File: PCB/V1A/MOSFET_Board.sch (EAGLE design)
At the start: 276 parts, among them IC301 7805T, IC302 7805T, J301 +12V, J302 FAN_MOLEX4PIN, J303 FAN_MOLEX4PIN, J304 DUT+, J305 DUT-, Q201 SIRC10DP, Q202 SIRC10DP, Q203 BC817, Q204 BC817, Q205 SIRC10DP, Q206 SIRC10DP, Q207 BC817, Q208 BC807, Q209 BC817, Q210 BC807, Q211 IXTK102N65X2, Q212 IXTK102N65X2, Q301 BC817, Q302 BC817, Q401 BC807, Q402 BC807, Q403 BC807, Q404 BC807, Q405 BC807, Q406 BC807, Q407 BC807, Q408 BC807, Q409 BC807, Q410 BC807, Q411 BC807, Q412 BC807, Q413 BC807, Q414 BC807, U1 LP2985-3.1, U201 AD420, U202 AD420, U203 LT1014I, U204 LT1014I, U205 AD620, U206 AD620, U207 AD620, U208 AD620, U209 LTC1865L, U210 LTC1865L, U301 LP2985-3.1, U302 LP2985-3.1, U303 AD620, U304 LTC1865L, U305 LTC1865L, U306 MAX743, U401 HCPL-063N, U402 HCPL-063N, U403 HCPL-063N, U404 HCPL-063N, U405 HCPL-063N, U406 HCPL-063N, U407 HCPL-063N

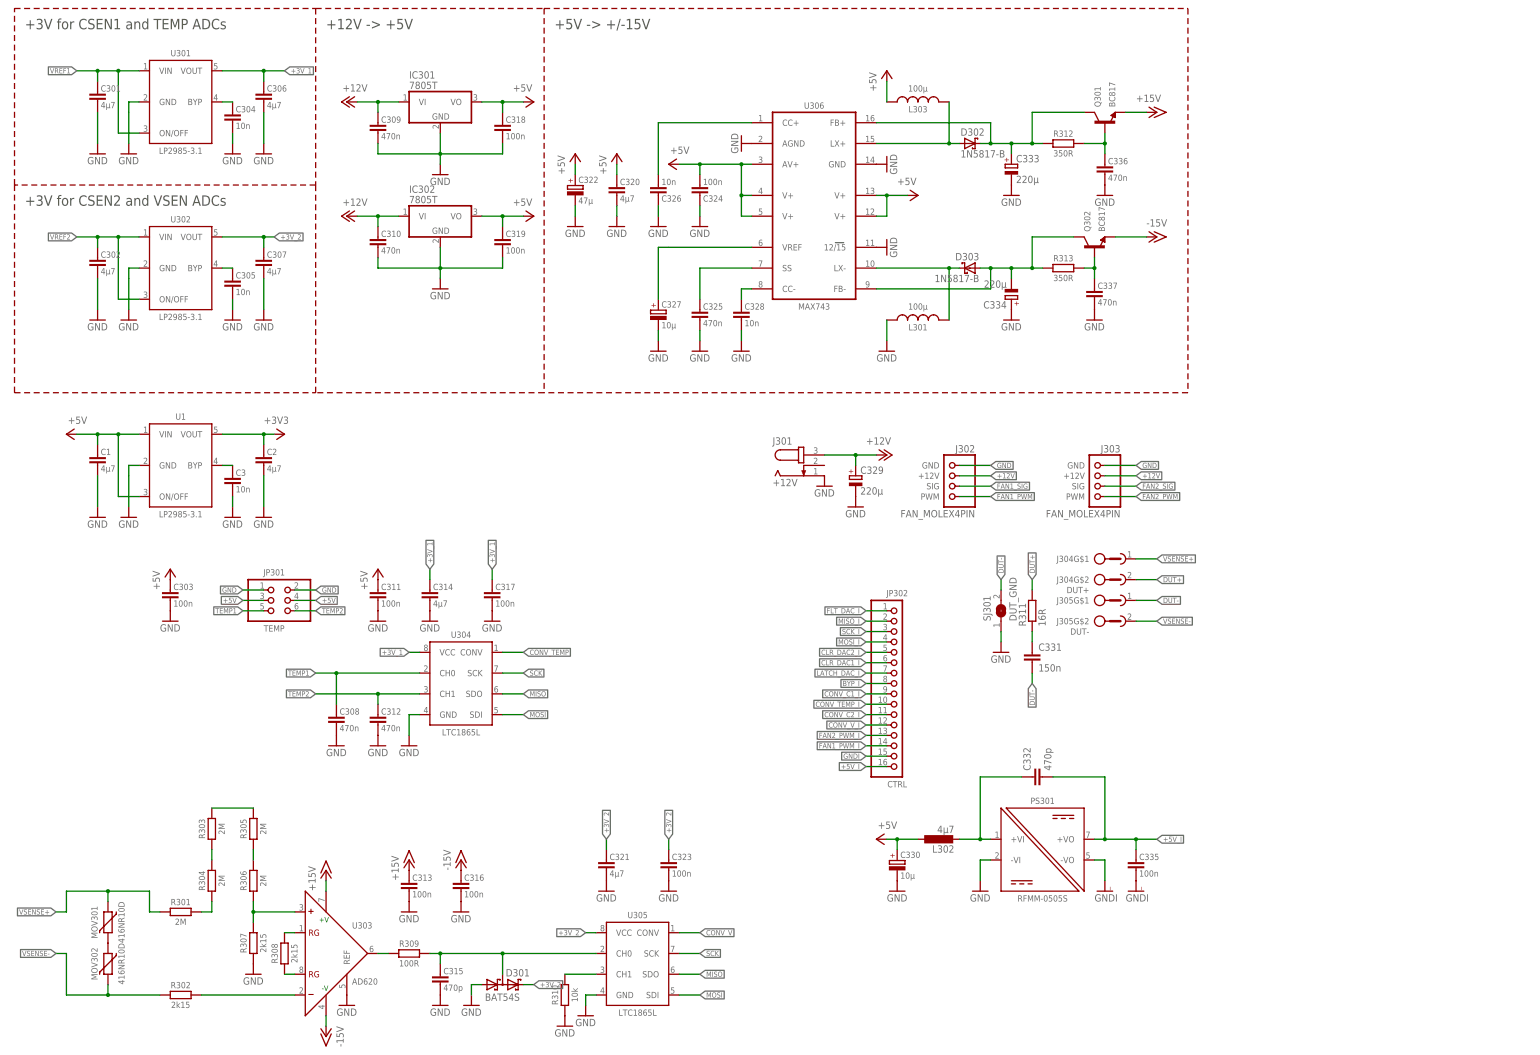
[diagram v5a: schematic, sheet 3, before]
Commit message: Finished first pass routing/layout
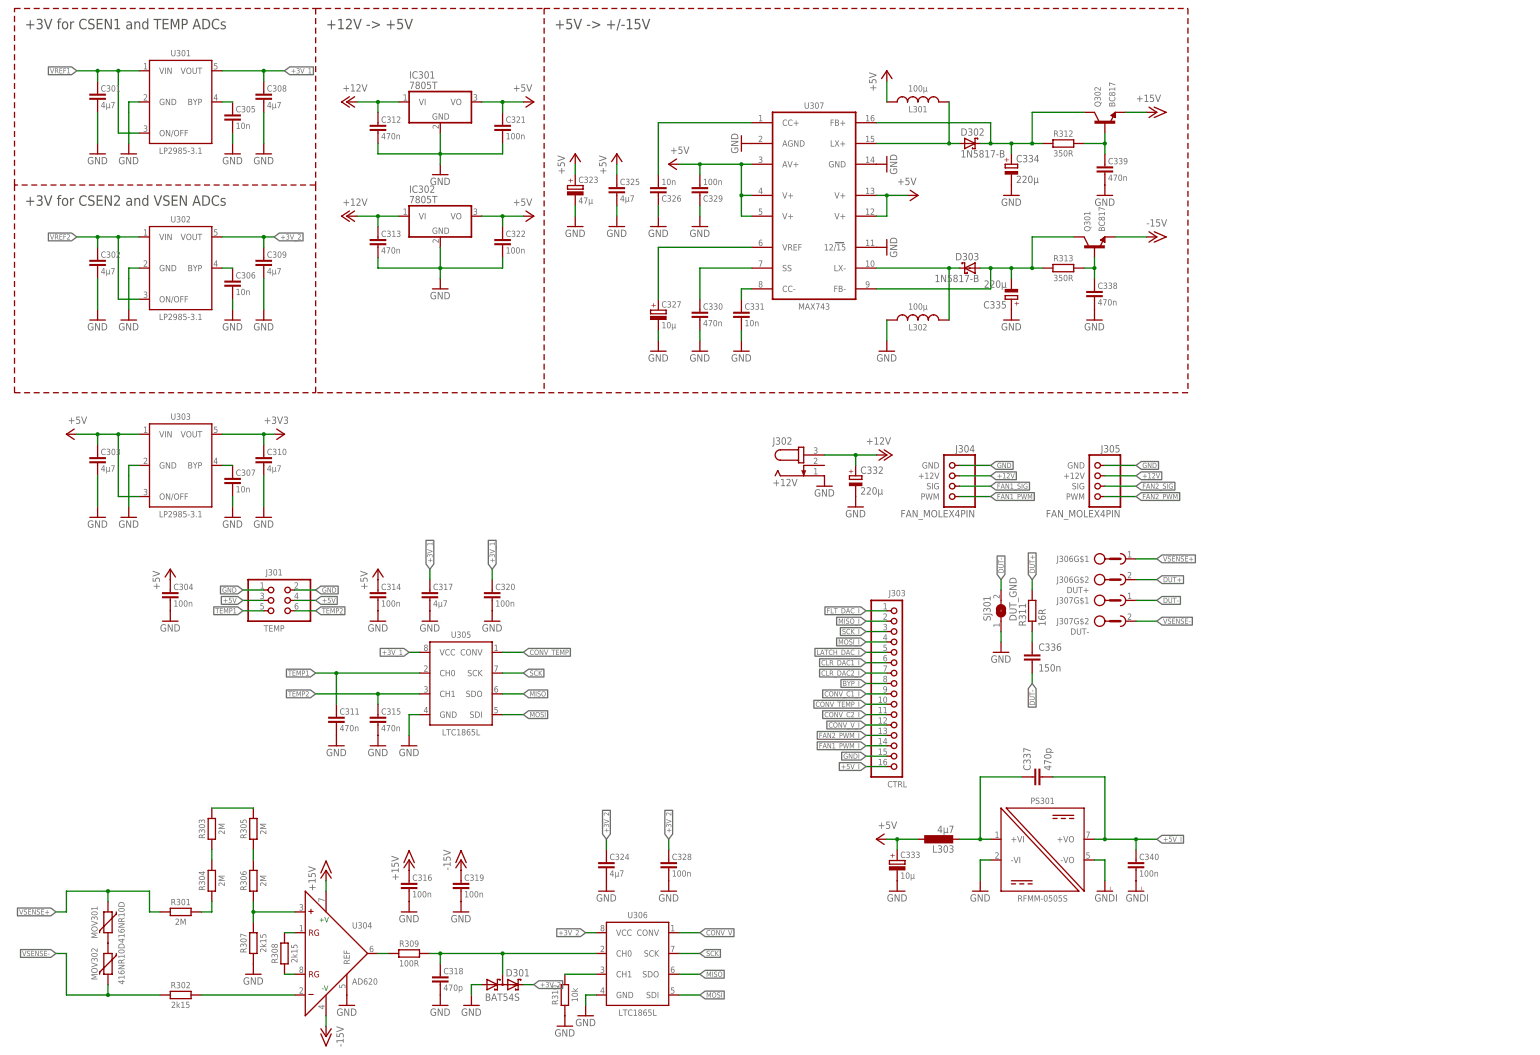
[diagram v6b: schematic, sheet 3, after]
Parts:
- removed C1, C2: 4µ7, passives:C-EU-3216
- removed C3: 10n, passives:C-EU-2012
- removed JP301: TEMP, mechanical:HEAD_2X3_MALE
- removed JP302: CTRL, mechanical:HEAD_1X16_MALE
- removed U1: LP2985-3.1, ic:LP2985-3.1
- added C338, C339: 470n, passives:C-EU-1608
- added C340: 100n, passives:C-EU-1608
- added J306: DUT+, mechanical:AMPHENOL_TERM-BLOCK_2
- added J307: DUT-, mechanical:AMPHENOL_TERM-BLOCK_2
- added U307: MAX743, ic:MAX743WE
- C303, C317, C324: value 100n -> 4µ7; device passives:C-EU-1608 -> passives:C-EU-3216
- C304, C328: value 10n -> 100n; device passives:C-EU-2012 -> passives:C-EU-1608
- C306, C307: value 4µ7 -> 10n; device passives:C-EU-3216 -> passives:C-EU-2012
- C308, C309, C310, C325: value 470n -> 4µ7; device passives:C-EU-1608 -> passives:C-EU-3216
- C311, C313: value 100n -> 470n
- C314, C320, C321: value 4µ7 -> 100n; device passives:C-EU-3216 -> passives:C-EU-1608
- C315: value 470p -> 470n
- C318: value 100n -> 470p
- C322: value 47µ -> 100n; device passives:CPOL-7343-DE -> passives:C-EU-1608
- C323: value 100n -> 47µ; device passives:C-EU-1608 -> passives:CPOL-7343-DE
- C329: value 220µ -> 100n; device rcl:CPOL-EUE3.5-10 -> passives:C-EU-1608
- C330: value 10µ -> 470n; device passives:CPOL-6032-C -> passives:C-EU-1608
- C331: value 150n -> 10n; device rcl:C-EU050-030X075 -> passives:C-EU-2012
- C332: value 470p -> 220µ; device rcl:C-EU075-032X103 -> rcl:CPOL-EUE3.5-10
- C333: value 220µ -> 10µ; device rcl:CPOL-EUE3.5-10 -> passives:CPOL-6032-C
- C335: value 100n -> 220µ; device passives:C-EU-1608 -> rcl:CPOL-EUE3.5-10
- C336: value 470n -> 150n; device passives:C-EU-1608 -> rcl:C-EU050-030X075
- C337: value 470n -> 470p; device passives:C-EU-1608 -> rcl:C-EU075-032X103
- J301: value +12V -> TEMP; device con-jack:JACK-PLUG1 -> mechanical:HEAD_2X3_MALE
- J302: value FAN_MOLEX4PIN -> +12V; device mechanical:FAN_MOLEX4PIN -> con-jack:JACK-PLUG1
- J303: value FAN_MOLEX4PIN -> CTRL; device mechanical:FAN_MOLEX4PIN -> mechanical:HEAD_1X16_MALE
- J304: value DUT+ -> FAN_MOLEX4PIN; device mechanical:AMPHENOL_TERM-BLOCK_2 -> mechanical:FAN_MOLEX4PIN
- J305: value DUT- -> FAN_MOLEX4PIN; device mechanical:AMPHENOL_TERM-BLOCK_2 -> mechanical:FAN_MOLEX4PIN
- L302: value 4µ7 -> 100µ; device inductor-coilcraft:MSS7341 -> passives:L-EU_MSS1260
- L303: value 100µ -> 4µ7; device passives:L-EU_MSS1260 -> inductor-coilcraft:MSS7341
- U303: value AD620 -> LP2985-3.1; device ic:AD620R-8 -> ic:LP2985-3.1
- U304: value LTC1865L -> AD620; device ic:LTC1865L -> ic:AD620R-8
- U306: value MAX743 -> LTC1865L; device ic:MAX743WE -> ic:LTC1865L
- renumbered HS1 to HS201, HS2 to HS202
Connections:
- net +12V: now also C312.1, C313.1, C332.+, J302.3, J304.+12V, J305.+12V; no longer C309.1, C310.1, C329.+, J301.3, J302.+12V, J303.+12V
- net +15V: now also C316.1, Q302.E, U304.+V; no longer C313.1, Q301.E, U303.+V
- net +3V3: now also C310.1, U303.VOUT; no longer C2.1, U1.VOUT
- net +3V_1: now also C308.1, C320.1, U305.VCC; no longer C306.1, C314.1, U304.VCC
- net +3V_2: now also C309.1, C324.1, C328.1, U306.VCC; no longer C307.1, C321.1, C323.1, U305.VCC
- net +5V: now also C304.1, C314.1, C321.1, C322.1, C323.+, C325.1, C329.2, C333.+, J301.3, J301.4, L301.1, L303.2, U303.ON/OFF, U303.VIN, U307.AV+, U307.V+, U307.V+@1, U307.V+@2, U307.V+@3; no longer C1.1, C311.1, C318.1, C319.1, C320.1, C322.+, C324.2, C330.+, JP301.3, JP301.4, L302.2, L303.1, U1.ON/OFF, U1.VIN, U306.AV+, U306.V+, U306.V+@1, U306.V+@2, U306.V+@3
- net +5V_I: now also C337.2, C340.1, J303.16; no longer C332.2, C335.1, JP302.16
- net -15V: now also C319.1, Q301.E, U304.-V; no longer C316.1, Q302.E, U303.-V
- net BYP_I: now also J303.8; no longer JP302.8
- net CLR_DAC1_I: now also J303.6; no longer JP302.6
- net CLR_DAC2: now also C413.1, R413.1, U401.VO2; no longer C427.1, R427.1, U406.VO2
- net CLR_DAC2_I: now also J303.7, Q405.B; no longer JP302.5, Q413.B
- net CONV_C1_I: now also J303.9; no longer JP302.9
- net CONV_C2_I: now also J303.11; no longer JP302.11
- net CONV_TEMP: now also U305.CONV; no longer U304.CONV
- net CONV_TEMP_I: now also J303.10; no longer JP302.10
- net CONV_V: now also U306.CONV; no longer U305.CONV
- net CONV_V_I: now also J303.12; no longer JP302.12
- net DUT+: now also J306G$2.1; no longer J304G$2.1
- net DUT-: now also C336.2, J307G$1.1; no longer C331.2, J305G$1.1
- net FAN1_PWM: now also J304.PWM; no longer J302.PWM
- net FAN1_PWM_I: now also J303.14; no longer JP302.14
- net FAN1_SIG: now also J304.SIG; no longer J302.SIG
- net FAN2_PWM: now also J305.PWM; no longer J303.PWM
- net FAN2_PWM_I: now also J303.13; no longer JP302.13
- net FAN2_SIG: now also J305.SIG; no longer J303.SIG
- net FLT_DAC_I: now also J303.1; no longer JP302.1
- net GND: now also C322.2, C323.-, C324.2, C329.1, C330.2, C331.2, C332.-, C334.-, C335.+, C338.2, C339.2, J301.2, J302.1, J304.GND, J305.GND, L302.2, U303.GND, U304.REF, U307.12/15, U307.AGND, U307.GND; no longer C1.2, C2.2, C3.2, C322.-, C323.2, C324.1, C329.-, C330.-, C334.+, C336.2, C337.2, J302.GND, J303.GND, JP301.1, JP301.2, L301.2, U1.GND, U303.REF, U304.GND, U306.12/15, U306.AGND
- net GNDI: now also C340.2, J303.15; no longer C335.2, JP302.15
- net LATCH_DAC: now also C427.1, R427.1, U406.VO2; no longer C413.1, R413.1, U401.VO2
- net LATCH_DAC_I: now also J303.5, Q413.B; no longer JP302.7, Q405.B
- net MISO: now also U306.SDO; no longer U304.SDO
- net MISO_I: now also J303.2; no longer JP302.2
- net MOSI: now also U306.SDI; no longer U304.SDI
- net MOSI_I: now also J303.4; no longer JP302.4
- net N$10: now also C305.1; no longer C304.1
- net N$23: now also U304.OUT; no longer U303.OUT
- net N$29: now also U304.+; no longer U303.+
- net N$30: now also C318.1, U306.CH0; no longer C315.1, U305.CH0
- net N$32: now also C334.+, Q302.C, U307.FB+; no longer C333.+, Q301.C, U306.FB+
- net N$34: now also C331.1, U307.CC-; no longer C328.1, U306.CC-
- net N$35: now also C330.1, U307.SS; no longer C325.1, U306.SS
- net N$36: now also U304.-; no longer U303.-
- net N$37: now also U307.CC+; no longer U306.CC+
- net N$38: now also L301.2, U307.LX+; no longer L303.2, U306.LX+
- net N$39: now also L302.1, U307.LX-; no longer L301.1, U306.LX-
- net N$45: now also U306.CH1; no longer U305.CH1
- net N$60: now also C337.1, L303.1; no longer C332.1, L302.1
- net N$61: now also C336.1; no longer C331.1
- net N$62: now also C306.1; no longer C305.1
- net N$63: now also C339.1, Q302.B; no longer C336.1, Q301.B
- net N$64: now also C335.-, Q301.C, U307.FB-; no longer C334.-, Q302.C, U306.FB-
- net N$65: now also C338.1, Q301.B; no longer C337.1, Q302.B
- net N$66: now also C307.1, U303.BYP; no longer C3.1, U1.BYP
- net RG1_H6: now also U304.RG@1; no longer U303.RG@1
- net RG2_H6: now also U304.RG@2; no longer U303.RG@2
- net SCK: now also U306.SCK; no longer U304.SCK
- net SCK_I: now also J303.3; no longer JP302.3
- net TEMP1: now also C311.1, J301.5, U305.CH0; no longer C308.1, JP301.5, U304.CH0
- net TEMP2: now also C315.1, J301.6, U305.CH1; no longer C312.1, JP301.6, U304.CH1
- net VREF_MAX743: now also U307.VREF; no longer U306.VREF
- net VSENSE+: now also J306G$1.1; no longer J304G$1.1
- net VSENSE-: now also J307G$2.1; no longer J305G$2.1
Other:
- moved on the sheet: C303, C304, C305, C306, C307, C308, C309, C310, C311, C312, C313, C314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
